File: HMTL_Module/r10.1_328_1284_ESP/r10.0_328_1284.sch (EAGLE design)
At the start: 43 parts, among them U2 ATMEGA328P_PDIP, Y1 16MHz

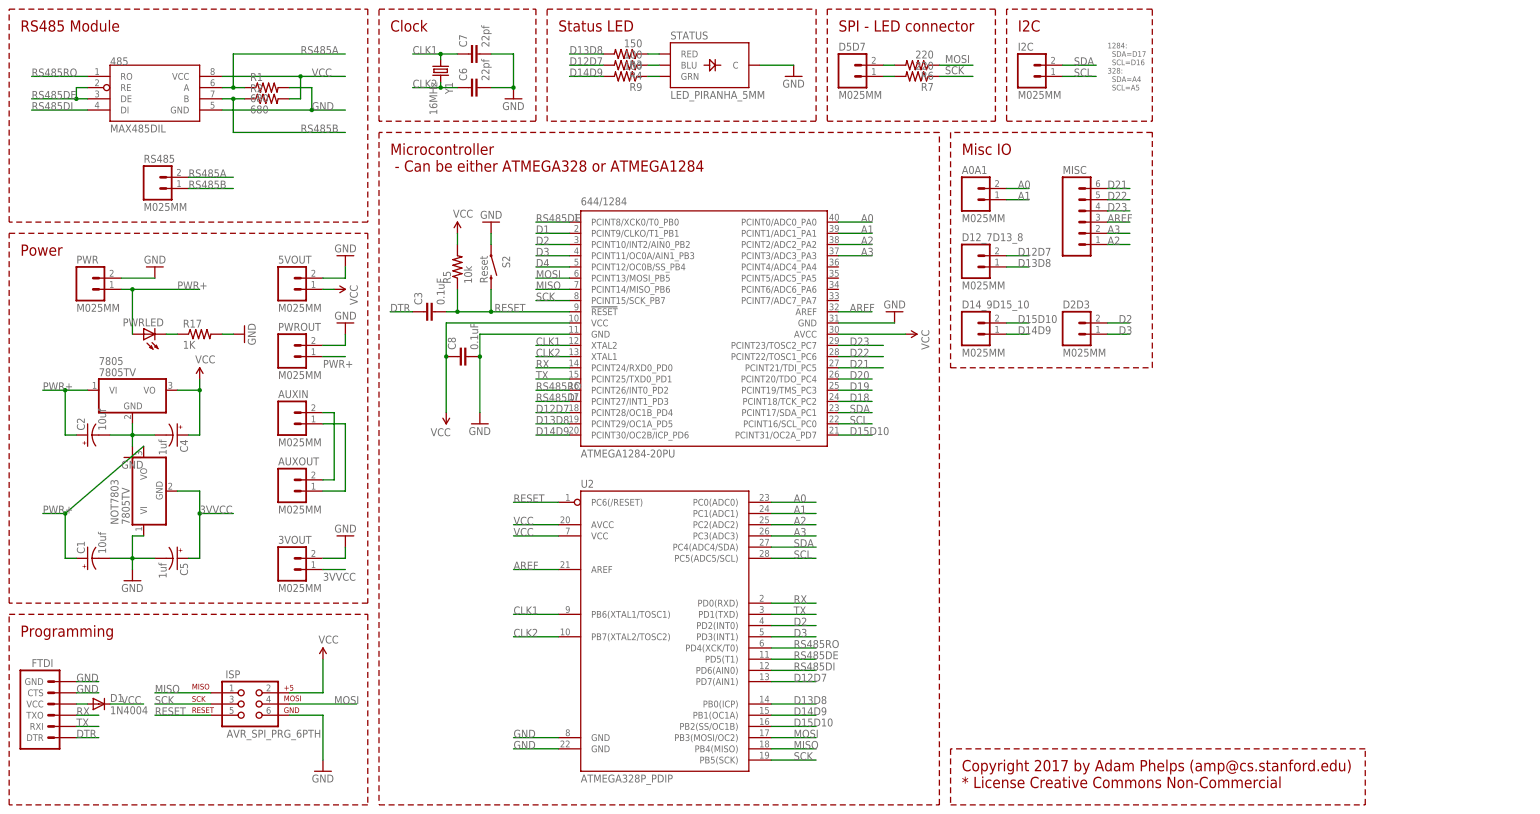
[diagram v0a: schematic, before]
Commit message: Added the ESP8266 module to r10.0_328_1284
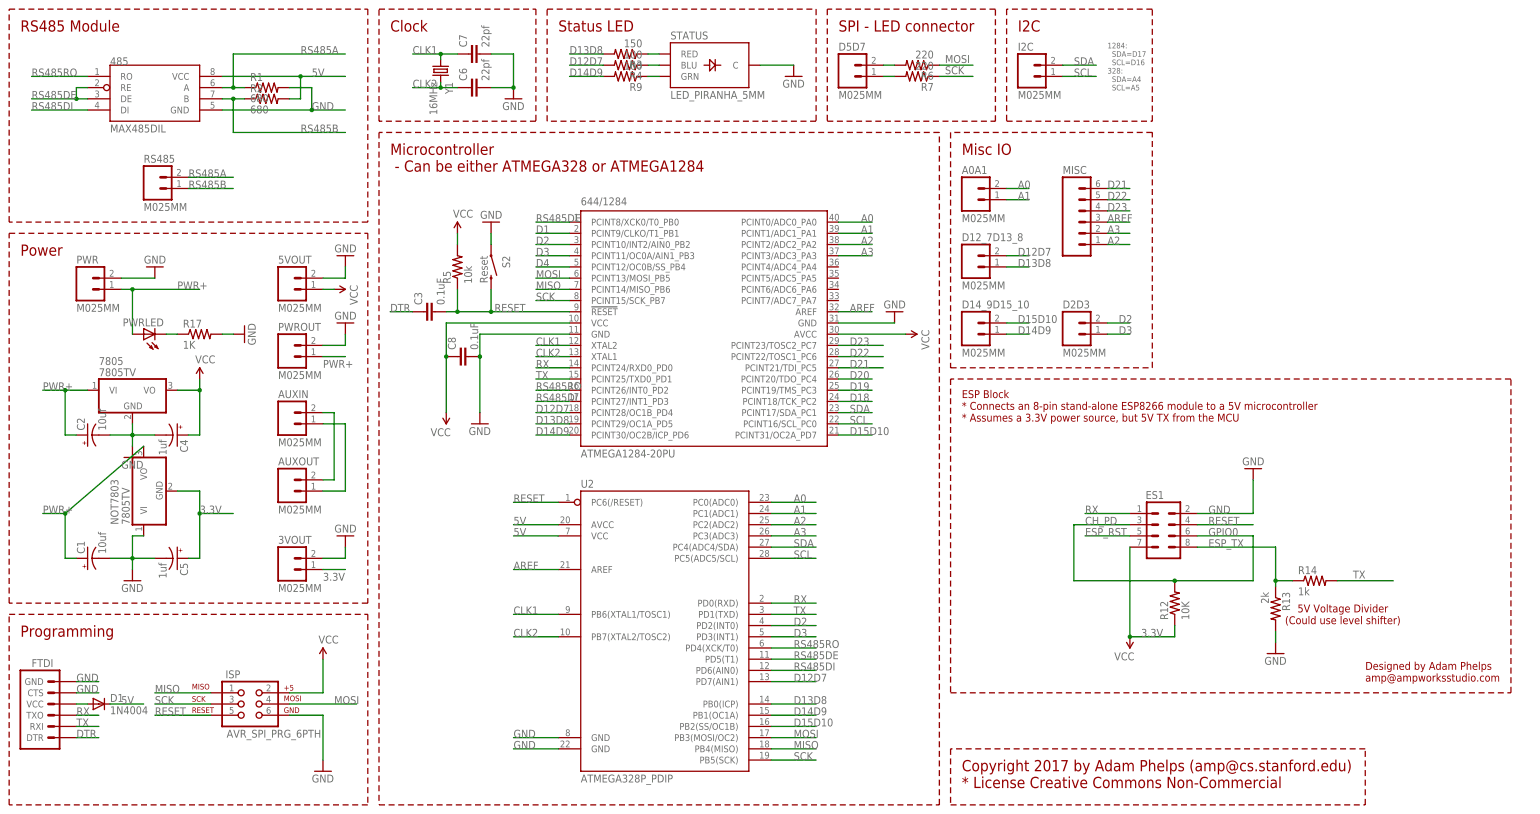
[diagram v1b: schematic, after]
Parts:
- added ES1: (no value), SparkFun-Connectors:M04X2
- added R12: 10K, SparkFun-Resistors:1KOHM-1/4W-1%(PTH)
- added R13: 2k, SparkFun-Resistors:1KOHM-1/4W-1%(PTH)
- added R14: 1k, SparkFun-Resistors:1KOHM-1/4W-1%(PTH)
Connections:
- net VCC renamed 5V
- removed net 3VVCC: 3VOUT.1, C5.+, NOT7803.GND
- new net 3.3V: 3VOUT.1, C5.+, ES1.7, NOT7803.GND, R12.1
- new net CH_PD: ES1.3, ES1.6, R12.2
- new net ESP_RST: ES1.5
- new net ESP_TX: ES1.8, R13.1, R14.1
- net GND: now also ES1.2, R13.2
- net RESET: now also ES1.4
- net RX: now also ES1.1
- net TX: now also R14.2
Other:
- note added: "5V Voltage Divider (Could use level shifter)"
- note added: "Designed by Adam Phelps amp@ampworksstudio.com"
- note added: "ESP Block * Connects an 8-pin stand-alone ESP8266 module to a 5V microcontroller * Assumes a 3.3V power source, but 5V TX from the MCU"
- note added: "GPIO0"
